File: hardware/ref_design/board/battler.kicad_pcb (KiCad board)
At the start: 2 copper layers, 71.4 x 127.7 mm, 159 parts, among them J1 TYPE-C-31-M-12, J2 53261-0271, J3 FH12-50S-0.5SH(55), J5 SWD, J6 UART, J7 DEBUG PADS, Q1 2N7002, Q5 AO3400A, Q6 AO3400A, Q7 2N7002, SW1 P1 UP, SW10 P2 DOWN, SW11 P2 LEFT, SW12 P2 RIGHT, SW13 P2 A, SW14 P2 B, SW15 P2 X, SW16 P2 Y, SW18 BOOTSEL, SW19 RESET, SW2 P1 DOWN, SW20 P1 SELECT, SW21 P1 START / PWR, SW22 P2 SELECT, SW23 P2 START / PWR, SW3 P1 LEFT, SW4 P1 RIGHT, SW5 P1 A, SW6 P1 B, SW7 P1 X, SW8 P1 Y, SW9 P2 UP, U1 SRV05-4, U2 BQ24073RGTR, U3 ME6211C33M5G, U4 RP2354B, U6 MCP6002, U8 SN74HC165PWR, U9 SN74HC165PWR, X1 12MHz

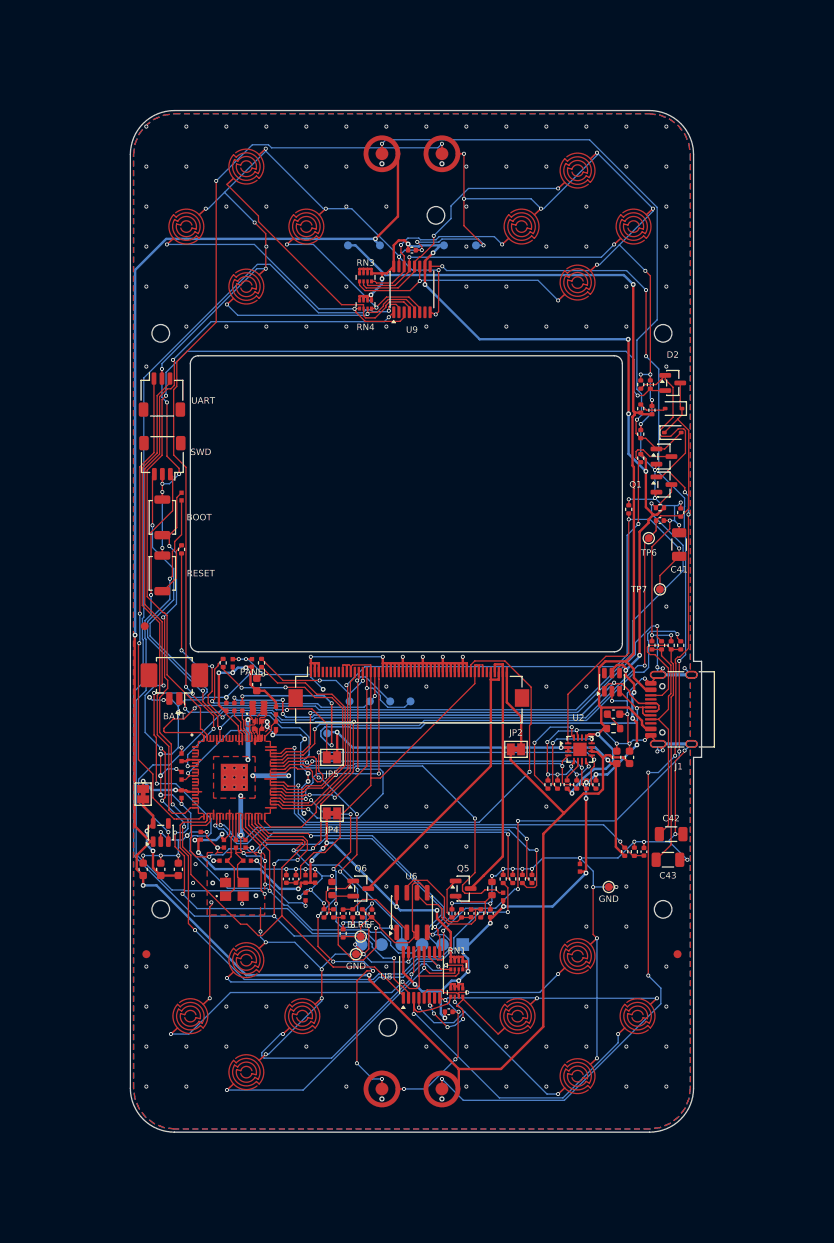
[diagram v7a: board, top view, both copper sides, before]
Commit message: ref_design: strips review: USB pair, SR_CLK series resistor, strip stitching, pinmap
Review of the strips beside the cell's hole (rows 1-4 of the review):
- USB D+/D-: route.py's usb_pair() draws them as one pair (0.2 mm, 0.3 apart) from
  J1 (D+ pads joined behind A7, D- at their tips) through U1, turned so each line
  runs over its own pin with no stub, then on the back to R21/R22. C1/R41 moved
  below the pair.
- SR_CLK: R65 (33 ohm, C25105, Basic) in series at the RP2354B's end, about 12 mm
  of track from pin 37, clear of the folded FPC. A 0.4 mm clock-to-SR_PL/SR_DATA
  clearance rule (and a GND guard track along each strip) left SR_CLK or SR_PL to
  U9 unrouted in five runs, so neither is in this board.
- Ground: strip_stitch() adds GND vias in the strips wherever both pours are filled.
- Flex: C47 turned with its long axis along the strip; the case asked for floor
  ribs under the strips (CELLCUT_FOR_CASE.md).
- docs/pinmap.md: both Starts as power buttons, SR_PL/SR_CLK/SR_DATA roles, the
  BQ24073 charger (no TP4056, CHG_DONE_N, D5/D7/Q2), 27 ohm USB resistors.

Routed clean (seed 7): DRC 0 errors, 0 unconnected; check_netlist, check_pins,
ERC pass; check_fit 17, the known case-side items.

Co-Authored-By: Claude Opus 5.5 <noreply@anthropic.com>
Claude-Session: https://claude.ai/code/session_01Y3mFMxLYqNeyyedvbYuRwX
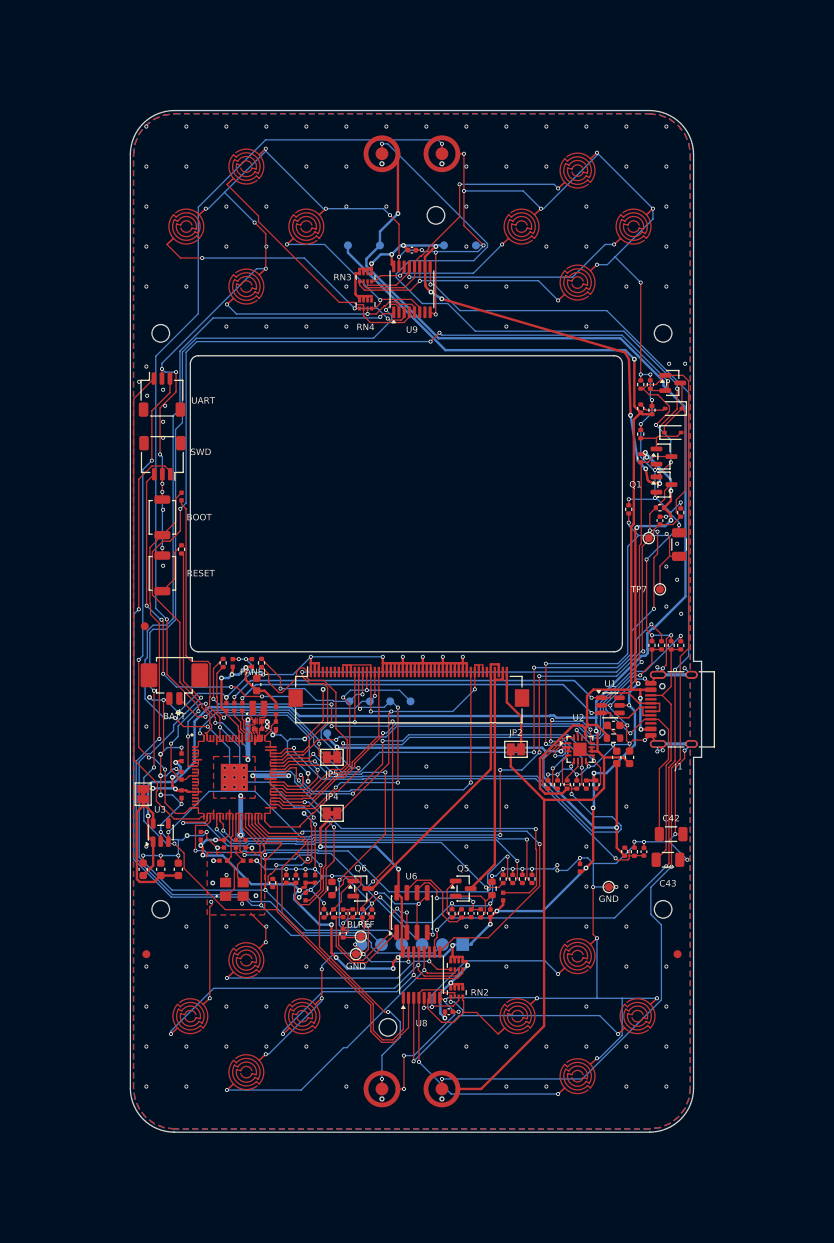
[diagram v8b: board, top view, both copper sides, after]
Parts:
- added R65: 33, Resistor_SMD:R_0402_1005Metric, F.Cu at (82.6, 132.7)
- moved U1 2.91 mm to (124.8, 110.5), turned to 0 degrees
- moved C1 1.40 mm to (125.2, 113.0)
- moved R41 1.20 mm to (125.2, 114.6)
- turned C47 to 90 degrees
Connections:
- U4 pad 37: SR_CLK -> SR_CLK_MCU
- U8 pad 2: SR_CLK -> /Buttons/SR_CLK
- U9 pad 2: SR_CLK -> /Buttons/SR_CLK
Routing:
- net SR_CLK: track 167.0 -> 0.00 mm, vias 5 -> 0
- net /Buttons/SR_CLK: track 0.00 -> 150.3 mm, vias 0 -> 4
- net SR_DATA: track 34.7 -> 58.5 mm
- net /MCU/REV0: track 67.8 -> 47.7 mm
- net CHG_OFF: track 42.6 -> 62.5 mm
- net SR_CLK_MCU: track 0.00 -> 18.3 mm, vias 0 -> 2
- net +3V3: track 297.5 -> 315.2 mm, vias 37 -> 42
- net LCD_RST: track 59.5 -> 42.0 mm
- net +1V1: track 49.3 -> 63.6 mm
- net /Display/BL_FB2: track 10.3 -> 22.5 mm, vias 0 -> 2
- net VSYS: track 242.9 -> 255.1 mm, vias 4 -> 3
- net /USB_Charger/CHG_TEMP: track 47.3 -> 59.0 mm, vias 2 -> 5
- net USB_DM: track 68.7 -> 57.0 mm, vias 4 -> 2
- net P2_START_RAW: track 76.5 -> 88.0 mm
- net BL_PWM: track 29.9 -> 40.9 mm
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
